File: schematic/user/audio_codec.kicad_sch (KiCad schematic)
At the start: 27 parts, among them U4 TLV320AIC3254IRHBR

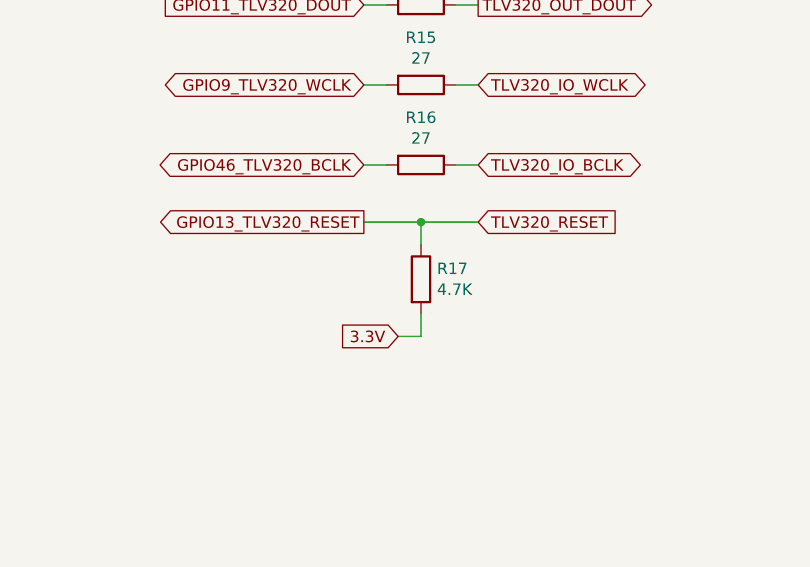
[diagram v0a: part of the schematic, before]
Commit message: v0.6 board: remove unneeded pullup for TLV320 reset pin (~370 uA->~50 uA deep sleep current savings).
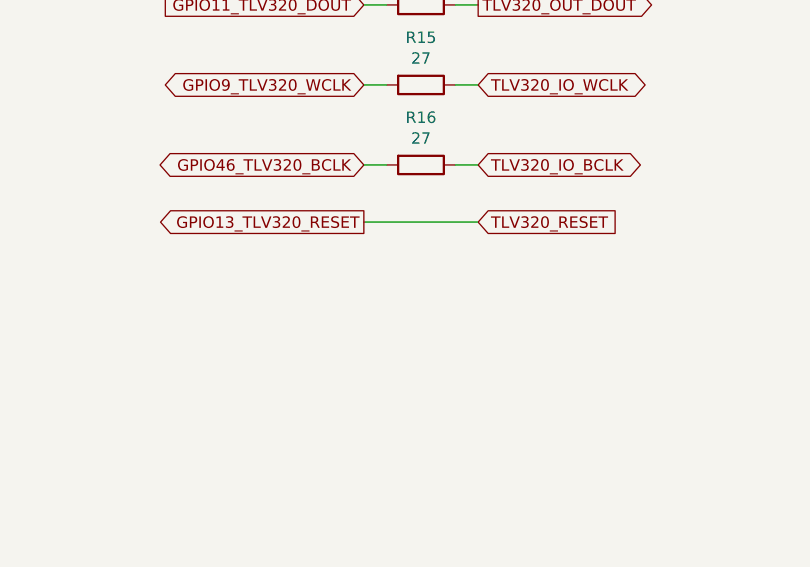
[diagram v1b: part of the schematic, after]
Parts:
- removed R17: 4.7K, Resistor_SMD:R_0603_1608Metric, symbol Device:R
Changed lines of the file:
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@@
   (junction (at 49.53 88.9) (diameter 0) (color 0 0 0 0)
-  )
-  (junction (at 224.79 132.08) (diameter 0) (color 0 0 0 0)
   )
   (junction (at 148.59 171.45) (diameter 0) (color 0 0 0 0)
@@
     (stroke (width 0) (type default) (color 0 0 0 0))
   )
-  (wire (pts (xy 224.79 144.78) (xy 224.79 142.24))
-    (stroke (width 0) (type default) (color 0 0 0 0))
-  )
   (wire (pts (xy 106.68 129.54) (xy 106.68 127))
     (stroke (width 0) (type default) (color 0 0 0 0))
@@
     (stroke (width 0) (type default) (color 0 0 0 0))
   )
-  (wire (pts (xy 222.25 144.78) (xy 224.79 144.78))
-    (stroke (width 0) (type default) (color 0 0 0 0))
-  )
   (polyline (pts (xy 156.21 193.04) (xy 21.59 193.04))
     (stroke (width 0) (type default) (color 0 0 0 0))
   )
-  (wire (pts (xy 218.44 132.08) (xy 224.79 132.08))
+  (wire (pts (xy 218.44 132.08) (xy 231.14 132.08))
     (stroke (width 0) (type default) (color 0 0 0 0))
   )
@@
     (stroke (width 0) (type default) (color 0 0 0 0))
   )
-  (wire (pts (xy 224.79 134.62) (xy 224.79 132.08))
-    (stroke (width 0) (type default) (color 0 0 0 0))
-  )
   (wire (pts (xy 53.34 88.9) (xy 49.53 88.9))
     (stroke (width 0) (type default) (color 0 0 0 0))
@@
   )
   (wire (pts (xy 49.53 91.44) (xy 53.34 91.44))
-    (stroke (width 0) (type default) (color 0 0 0 0))
-  )
-  (wire (pts (xy 224.79 132.08) (xy 231.14 132.08))
     (stroke (width 0) (type default) (color 0 0 0 0))
   )
@@
   (global_label "TLV320_OUT_USER" (shape output) (at 106.68 71.12 0) (fields_autoplaced)
     (effects (font (size 1.27 1.27)) (justify left))
-    (property "Intersheet References" "${INTERSHEET_REFS}" (id 0) (at -2.54 7.62 0)
-      (effects (font (size 1.27 1.27)) hide)
-    )
-  )
-  (global_label "3.3V" (shape input) (at 222.25 144.78 180) (fields_autoplaced)
-    (effects (font (size 1.27 1.27)) (justify right))
     (property "Intersheet References" "${INTERSHEET_REFS}" (id 0) (at -2.54 7.62 0)
       (effects (font (size 1.27 1.27)) hide)
@@
       (effects (font (size 1.27 1.27)) hide)
     )
-    (pin "1")
-    (pin "2")
-  )
-  (symbol (lib_id "Device:R") (at 224.79 138.43 0) (unit 1)
-    (in_bom yes) (on_board yes)
-    (property "Reference" "R17" (id 0) (at 226.568 137.2616 0)
-      (effects (font (size 1.27 1.27)) (justify left))
-    )
-    (property "Value" "4.7K" (id 1) (at 226.568 139.573 0)
-      (effects (font (size 1.27 1.27)) (justify left))
-    )
-    (property "Footprint" "Resistor_SMD:R_0603_1608Metric" (id 2) (at 223.012 138.43 90)
-      (effects (font (size 1.27 1.27)) hide)
-    )
-    (property "Datasheet" "https://datasheet.lcsc.com/lcsc/1810231411_YAGEO-RC0603FR-074K7L_C99782.pdf" (id 3) (at 224.79 138.43 0)
-      (effects (font (size 1.27 1.27)) hide)
-    )
-    (property "LCSC" "C99782" (id 4) (at 224.79 138.43 0)
-      (effects (font (size 1.27 1.27)) hide)
-    )

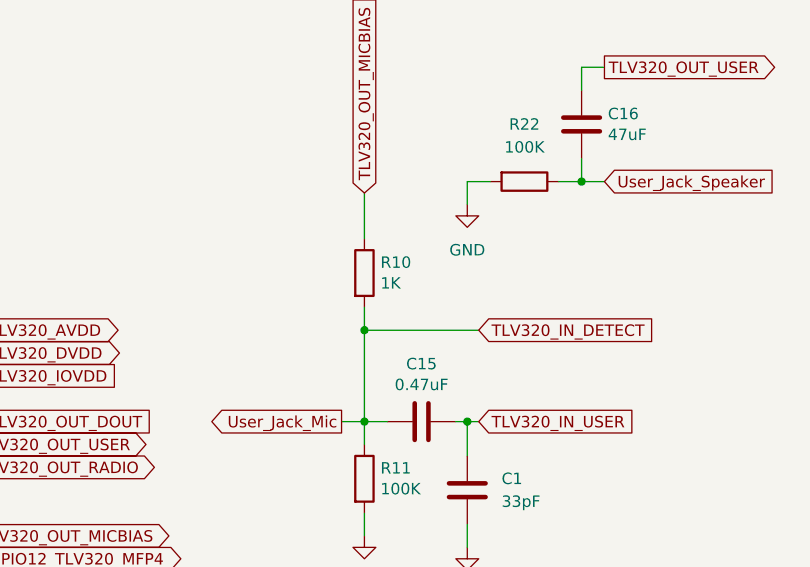
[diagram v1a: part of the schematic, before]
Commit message: v0.6 board: Increase mic bias resistor to 2.7K to match TLV320 datasheet.
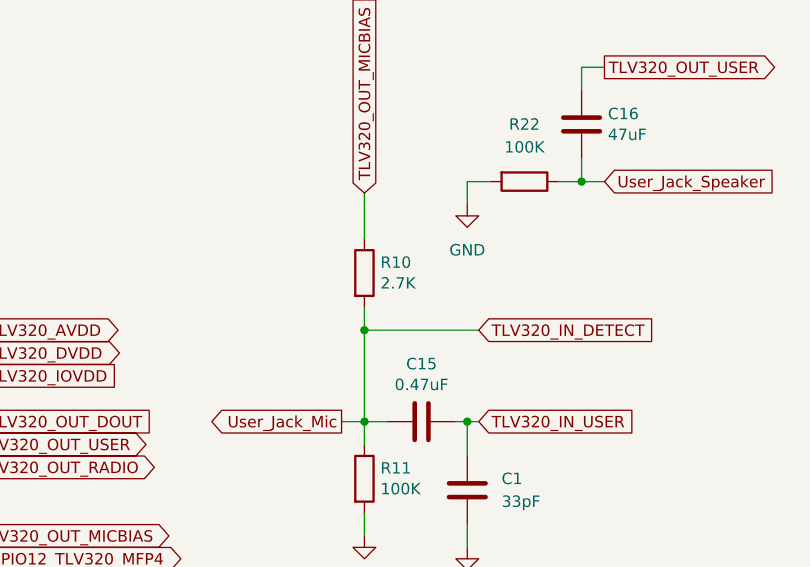
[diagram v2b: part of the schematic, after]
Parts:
- R10: value 1K -> 2.7K; LCSC C85373 -> C138017
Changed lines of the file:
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@@
       (effects (font (size 1.27 1.27)) (justify left))
     )
-    (property "Value" "1K" (id 1) (at 151.638 53.213 0)
+    (property "Value" "2.7K" (id 1) (at 151.638 53.213 0)
       (effects (font (size 1.27 1.27)) (justify left))
     )
@@
       (effects (font (size 1.27 1.27)) hide)
     )
-    (property "Datasheet" "https://datasheet.lcsc.com/lcsc/2110260430_UNI-ROYAL-Uniroyal-Elec-0402WGF1021TCE_C85373.pdf" (id 3) (at 149.86 52.07 0)
+    (property "Datasheet" "https://datasheet.lcsc.com/lcsc/1810241334_YAGEO-RC0402FR-072K7L_C138017.pdf" (id 3) (at 149.86 52.07 0)
       (effects (font (size 1.27 1.27)) hide)
     )
-    (property "LCSC" "C85373" (id 4) (at 149.86 52.07 0)
+    (property "LCSC" "C138017" (id 4) (at 149.86 52.07 0)
       (effects (font (size 1.27 1.27)) hide)
     )

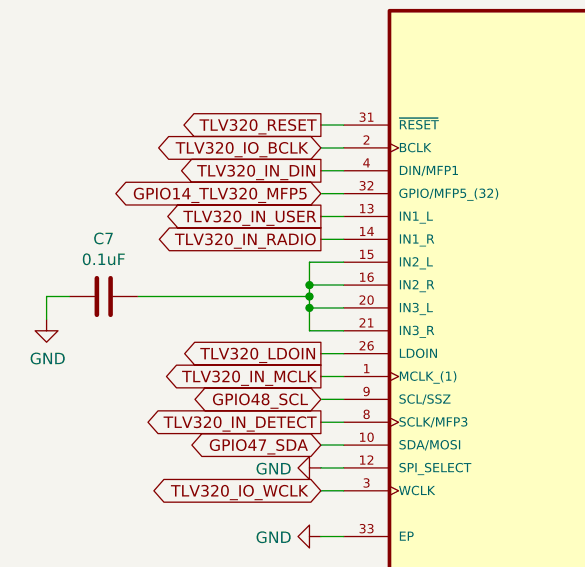
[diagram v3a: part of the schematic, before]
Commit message: v0.6 board: more tweaking of traces.
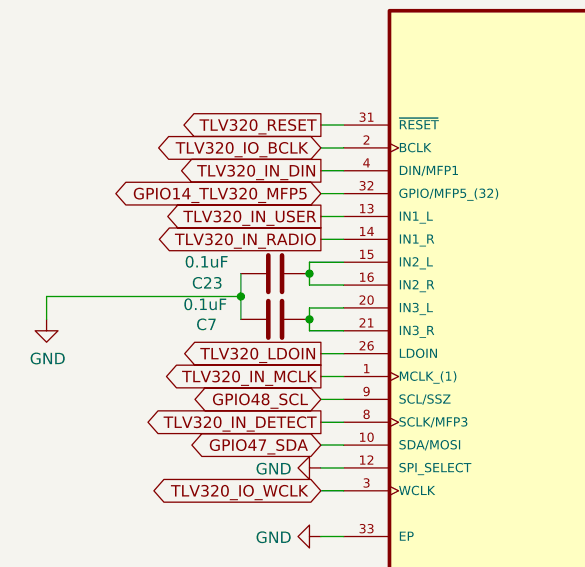
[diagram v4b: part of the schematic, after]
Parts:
- added C23: 0.1uF, Capacitor_SMD:C_0402_1005Metric, symbol Device:C
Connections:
- net GND: now also C23.2
- net at C7.1, U4.15 (IN2_L), U4.16 (IN2_R): no longer U4.20 (IN3_L), U4.21 (IN3_R)
- new net: C23.1, U4.20 (IN3_L), U4.21 (IN3_R)
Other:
- moved on the sheet: C7
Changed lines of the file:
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@@
     (company "FreeDV Project")
   )
-  (junction (at 49.53 88.9) (diameter 0) (color 0 0 0 0)
-  )
   (junction (at 148.59 171.45) (diameter 0) (color 0 0 0 0)
   )
   (junction (at 50.8 167.64) (diameter 0) (color 0 0 0 0)
   )
-  (junction (at 49.53 86.36) (diameter 0) (color 0 0 0 0)
-  )
-  (junction (at 49.53 87.63) (diameter 0) (color 0 0 0 0)
+  (junction (at 41.91 87.63) (diameter 0) (color 0 0 0 0)
   )
   (junction (at 39.37 177.8) (diameter 0) (color 0 0 0 0)
@@
   (junction (at 149.86 68.58) (diameter 0) (color 0 0 0 0)
   )
+  (junction (at 49.53 90.17) (diameter 0) (color 0 0 0 0)
+  )
   (junction (at 149.86 58.42) (diameter 0) (color 0 0 0 0)
   )
@@
   )
   (junction (at 81.28 173.99) (diameter 0) (color 0 0 0 0)
+  )
+  (junction (at 49.53 85.09) (diameter 0) (color 0 0 0 0)
   )
   (no_connect (at 104.14 78.74))
@@
     (stroke (width 0) (type default) (color 0 0 0 0))
   )
-  (wire (pts (xy 49.53 86.36) (xy 49.53 87.63))
-    (stroke (width 0) (type default) (color 0 0 0 0))
-  )
   (wire (pts (xy 147.32 68.58) (xy 149.86 68.58))
     (stroke (width 0) (type default) (color 0 0 0 0))
@@
     (stroke (width 0) (type default) (color 0 0 0 0))
   )
+  (wire (pts (xy 49.53 85.09) (xy 49.53 86.36))
+    (stroke (width 0) (type default) (color 0 0 0 0))
+  )
   (wire (pts (xy 149.86 55.88) (xy 149.86 58.42))
     (stroke (width 0) (type default) (color 0 0 0 0))
@@
     (stroke (width 0) (type default) (color 0 0 0 0))
   )
-  (wire (pts (xy 22.86 87.63) (xy 20.32 87.63))
+  (wire (pts (xy 20.32 87.63) (xy 41.91 87.63))
     (stroke (width 0) (type default) (color 0 0 0 0))
   )
@@
     (stroke (width 0) (type default) (color 0 0 0 0))
   )
-  (wire (pts (xy 49.53 87.63) (xy 49.53 88.9))
-    (stroke (width 0) (type default) (color 0 0 0 0))
-  )
   (wire (pts (xy 245.11 27.94) (xy 242.57 27.94))
     (stroke (width 0) (type default) (color 0 0 0 0))
@@
     (stroke (width 0) (type default) (color 0 0 0 0))
   )
+  (wire (pts (xy 41.91 87.63) (xy 41.91 90.17))
+    (stroke (width 0) (type default) (color 0 0 0 0))
+  )
   (wire (pts (xy 53.34 119.38) (xy 50.8 119.38))
     (stroke (width 0) (type default) (color 0 0 0 0))
@@
     (stroke (width 0) (type default) (color 0 0 0 0))
   )
+  (wire (pts (xy 49.53 90.17) (xy 49.53 91.44))
+    (stroke (width 0) (type default) (color 0 0 0 0))
+  )
   (wire (pts (xy 50.8 167.64) (xy 48.26 167.64))
     (stroke (width 0) (type default) (color 0 0 0 0))
@@
     (stroke (width 0) (type default) (color 0 0 0 0))
   )
-  (wire (pts (xy 30.48 87.63) (xy 49.53 87.63))
-    (stroke (width 0) (type default) (color 0 0 0 0))
-  )
   (wire (pts (xy 160.02 68.58) (xy 161.29 68.58))
     (stroke (width 0) (type default) (color 0 0 0 0))
@@
     (stroke (width 0) (type default) (color 0 0 0 0))
   )
-  (wire (pts (xy 49.53 88.9) (xy 49.53 91.44))
+  (wire (pts (xy 49.53 88.9) (xy 49.53 90.17))
     (stroke (width 0) (type default) (color 0 0 0 0))
   )
@@
     (stroke (width 0) (type default) (color 0 0 0 0))
   )
+  (wire (pts (xy 41.91 87.63) (xy 41.91 85.09))
+    (stroke (width 0) (type default) (color 0 0 0 0))
+  )
   (wire (pts (xy 53.34 114.3) (xy 50.8 114.3))
     (stroke (width 0) (type default) (color 0 0 0 0))
@@
     (stroke (width 0) (type default) (color 0 0 0 0))
   )
-  (wire (pts (xy 49.53 83.82) (xy 49.53 86.36))
+  (wire (pts (xy 49.53 83.82) (xy 49.53 85.09))
     (stroke (width 0) (type default) (color 0 0 0 0))
   )
@@
     (pin "2")
   )
+  (symbol (lib_id "Device:C") (at 45.72 90.17 270) (unit 1)
+    (in_bom yes) (on_board yes)
+    (property "Reference" "C23" (id 0) (at 38.1821 86.1653 90))
+    (property "Value" "0.1uF" (id 1) (at 38.1 83.82 90))
+    (property "Footprint" "Capacitor_SMD:C_0402_1005Metric" (id 2) (at 41.91 91.1352 0)
+      (effects (font (size 1.27 1.27)) hide)
+    )
+    (property "Datasheet" "https://datasheet.lcsc.com/lcsc/1810191219_Samsung-Electro-Mechanics-CL05B104KO5NNNC_C1525.pdf" (id 3) (at 45.72 90.17 0)
+      (effects (font (size 1.27 1.27)) hide)
+    )
+    (property "LCSC" "C1525" (id 4) (at 45.72 90.17 0)
+      (effects (font (size 1.27 1.27)) hide)
+    )
+    (pin "1")
+    (pin "2")
+  )
   (symbol (lib_id "power:GND") (at 148.59 184.15 0) (unit 1)
     (in_bom yes) (on_board yes)
@@
     (pin "2")
   )
-  (symbol (lib_id "Device:C") (at 26.67 87.63 270) (unit 1)
-    (in_bom yes) (on_board yes)
-    (property "Reference" "C7" (id 0) (at 26.67 81.2292 90))
-    (property "Value" "0.1uF" (id 1) (at 26.67 83.5406 90))
-    (property "Footprint" "Capacitor_SMD:C_0402_1005Metric" (id 2) (at 22.86 88.5952 0)
-      (effects (font (size 1.27 1.27)) hide)
-    )
-    (property "Datasheet" "https://datasheet.lcsc.com/lcsc/1810191219_Samsung-Electro-Mechanics-CL05B104KO5NNNC_C1525.pdf" (id 3) (at 26.67 87.63 0)
-      (effects (font (size 1.27 1.27)) hide)
-    )
-    (property "LCSC" "C1525" (id 4) (at 26.67 87.63 0)
-      (effects (font (size 1.27 1.27)) hide)
-    )
+  (symbol (lib_id "Device:C") (at 45.72 85.09 270) (unit 1)
+    (in_bom yes) (on_board yes)
+    (property "Reference" "C7" (id 0) (at 38.1053 90.7737 90))
+    (property "Value" "0.1uF" (id 1) (at 37.9517 88.5463 90))
+    (property "Footprint" "Capacitor_SMD:C_0402_1005Metric" (id 2) (at 41.91 86.0552 0)
+      (effects (font (size 1.27 1.27)) hide)
+    )
+    (property "Datasheet" "https://datasheet.lcsc.com/lcsc/1810191219_Samsung-Electro-Mechanics-CL05B104KO5NNNC_C1525.pdf" (id 3) (at 45.72 85.09 0)
+      (effects (font (size 1.27 1.27)) hide)
+    )
+    (property "LCSC" "C1525" (id 4) (at 45.72 85.09 0)
+      (effects (font (size 1.27 1.27)) hide)
+    )

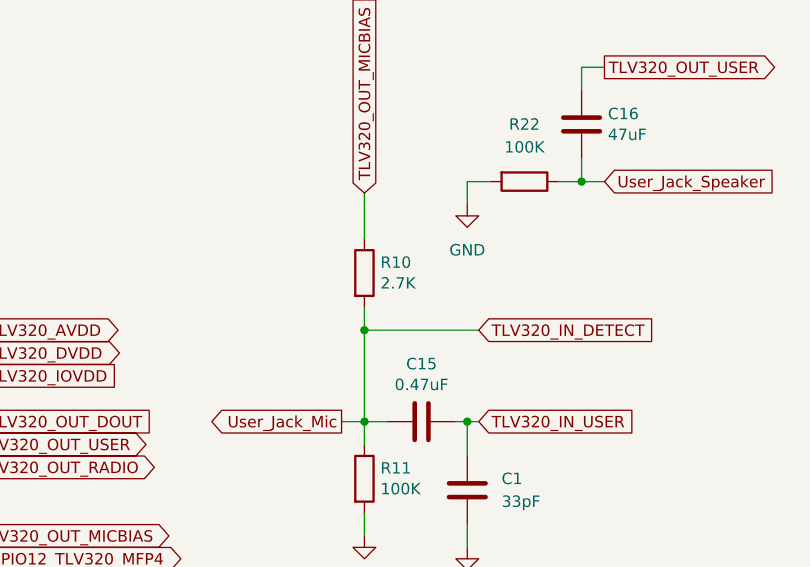
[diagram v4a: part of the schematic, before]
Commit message: v0.6 board: use 2.2K for microphone bias resistor.
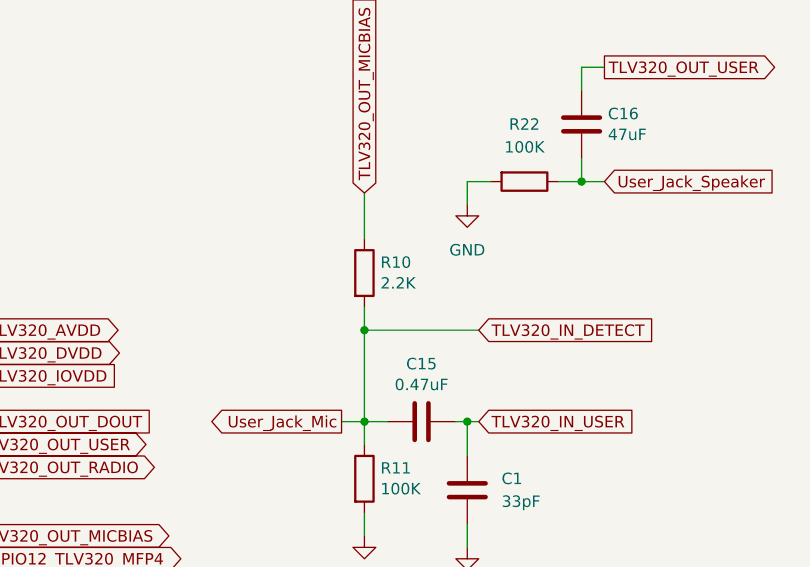
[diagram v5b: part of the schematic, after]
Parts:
- R10: value 2.7K -> 2.2K; LCSC C138017 -> C114762
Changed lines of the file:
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@@
       (effects (font (size 1.27 1.27)) (justify left))
     )
-    (property "Value" "2.7K" (id 1) (at 151.638 53.213 0)
+    (property "Value" "2.2K" (id 1) (at 151.638 53.213 0)
       (effects (font (size 1.27 1.27)) (justify left))
     )
@@
       (effects (font (size 1.27 1.27)) hide)
     )
-    (property "Datasheet" "https://datasheet.lcsc.com/lcsc/1810241334_YAGEO-RC0402FR-072K7L_C138017.pdf" (id 3) (at 149.86 52.07 0)
+    (property "Datasheet" "https://datasheet.lcsc.com/lcsc/1809201112_YAGEO-RC0402FR-072K2L_C114762.pdf" (id 3) (at 149.86 52.07 0)
       (effects (font (size 1.27 1.27)) hide)
     )
-    (property "LCSC" "C138017" (id 4) (at 149.86 52.07 0)
+    (property "LCSC" "C114762" (id 4) (at 149.86 52.07 0)
       (effects (font (size 1.27 1.27)) hide)
     )
